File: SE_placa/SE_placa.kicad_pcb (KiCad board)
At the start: 2 copper layers, 142.2 x 71.1 mm, 58 parts, among them J1 Bateria 3.3V, J3 Conn_02x07_ESP32_IO, J4 Conn_02x03_LORA_IO, J5 UART, J6 U.FL-R-SMT(01), J7 I2C-0, J8 I2C-1, J9 Micro_SD_Card_Det_Hirose_DM3AT, Q1 BSS138, Q2 BSS138, SW1 SW_Push_Download, SW2 SW_Push_ESP_RST, U1 ESP32-WROVER, U2 RFM95W-915S2

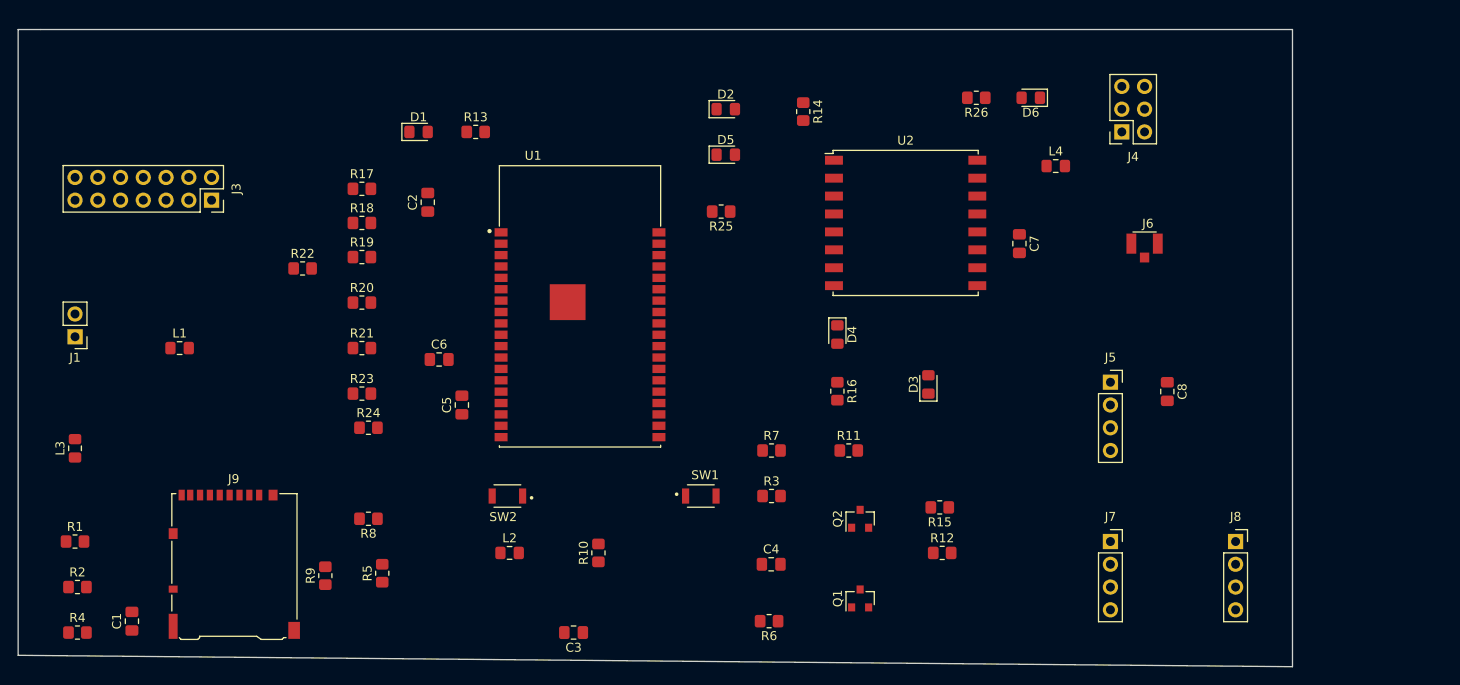
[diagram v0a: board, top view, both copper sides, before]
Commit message: Actualizacion de PCB solo rutas
Eliminado un led repetido, el led 5. Primer intento crudo de desarrollar la PCB sin estandares, tamaños de caminos u otras consideraciones tecnicas, solo ruteo para ir entendiendo y aprendiendo cual es la mejor ubicacion de los elementos, tambien saber si puedo llegar en algun momento a la meta de 52 mm X 40 mm.
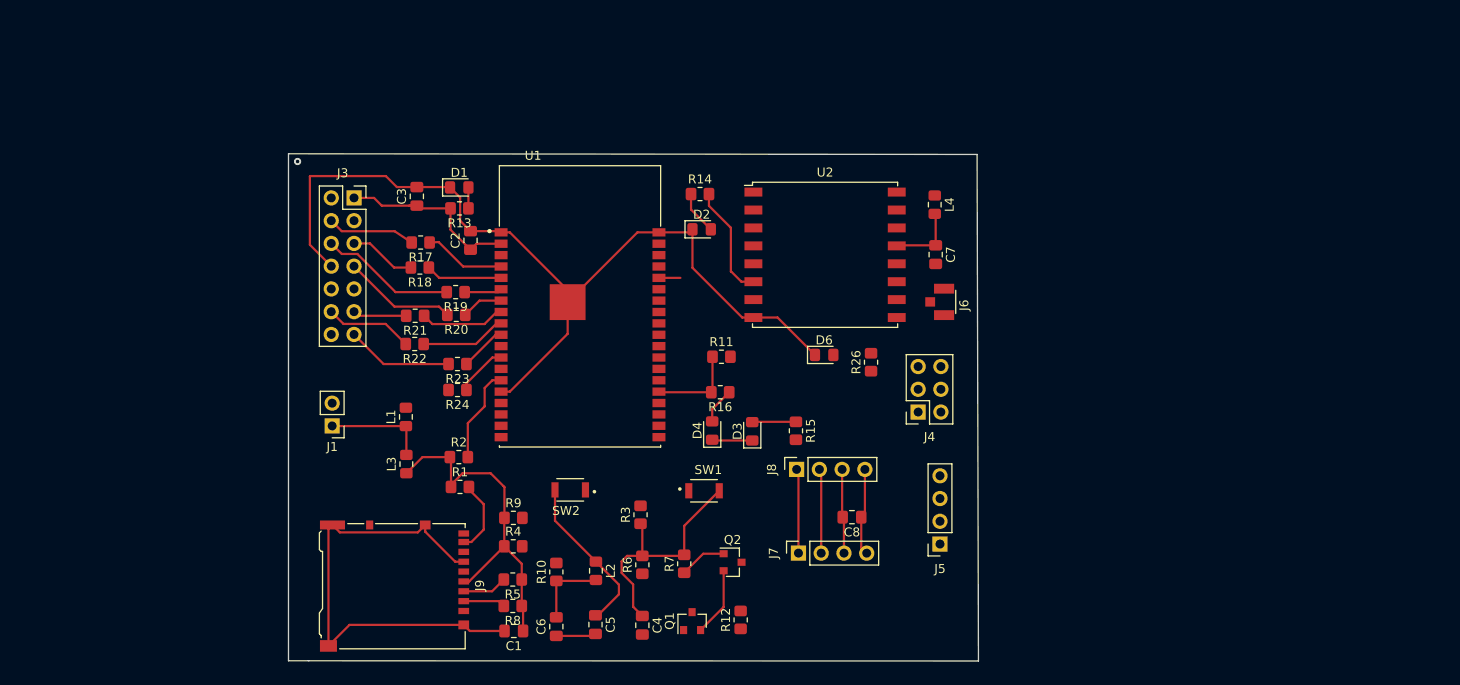
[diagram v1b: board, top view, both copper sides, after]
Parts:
- removed D5: LED, LED_SMD:LED_0805_2012Metric_Pad1.15x1.40mm_HandSolder
- removed R25: 2K, Resistor_SMD:R_0805_2012Metric_Pad1.20x1.40mm_HandSolder
- moved C3 51.7 mm to (138.5, 37.7), turned to 90 degrees
- moved J8 49.7 mm to (180.9, 68.1), turned to 90 degrees
- moved R4 49.6 mm to (149.2, 76.7)
- moved R2 45.0 mm to (143.2, 66.8)
- moved R1 43.4 mm to (143.3, 70.1)
- moved C1 42.6 mm to (149.3, 86.2), turned to 180 degrees
- moved J4 38.7 mm to (194.4, 61.7)
- moved C8 37.9 mm to (187.0, 73.5), turned to 180 degrees
- moved L3 37.0 mm to (137.3, 67.6)
- moved D6 36.8 mm to (183.9, 55.4), turned to 0 degrees
- moved J7 34.8 mm to (181.1, 77.5), turned to 90 degrees
- moved C6 32.6 mm to (154.1, 85.7), turned to 90 degrees
- moved R26 31.8 mm to (189.2, 56.2), turned to 90 degrees
- moved J1 30.4 mm to (129.0, 63.3)
- moved C5 28.7 mm to (158.4, 85.5), turned to 270 degrees
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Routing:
- net GND: track 0.00 -> 179.4 mm
- net Net-(C1-Pad1): track 0.00 -> 39.7 mm
- net /VCC-ESP: track 0.00 -> 31.3 mm
- net Net-(C4-Pad1): track 0.00 -> 26.8 mm
- net Net-(C5-Pad1): track 0.00 -> 18.2 mm
- net /IO34-I34: track 0.00 -> 15.1 mm
- net /IO35-I35: track 0.00 -> 12.7 mm
- net /SPI1-RST: track 0.00 -> 12.6 mm
- net /IO25: track 0.00 -> 11.9 mm
- net +3V3: track 0.00 -> 11.5 mm
- net /SPI2-MISO: track 0.00 -> 10.7 mm
- net /IO2: track 0.00 -> 9.89 mm
- net /IO36-I36: track 0.00 -> 9.84 mm
- net /IO33: track 0.00 -> 9.81 mm
- net Net-(R22-Pad1): track 0.00 -> 9.60 mm
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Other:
- board size 142.2 x 71.1 mm -> 77 x 56.6 mm

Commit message: reinicio de ruteo
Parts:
- moved L3 4.63 mm to (132.7, 67.1)
- moved L1 4.56 mm to (132.7, 62.3)
- moved R10 1.51 mm to (154.1, 81.1)
- moved R2 0.68 mm to (143.2, 66.1)
- moved C3 0.43 mm to (138.5, 38.1)
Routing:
- net GND: track 179.4 -> 0.00 mm
- net Net-(C1-Pad1): track 39.7 -> 0.00 mm
- net /VCC-ESP: track 31.3 -> 0.00 mm
- net Net-(C4-Pad1): track 26.8 -> 0.00 mm
- net Net-(C5-Pad1): track 18.2 -> 0.00 mm
- net /IO34-I34: track 15.1 -> 0.00 mm
- net /IO35-I35: track 12.7 -> 0.00 mm
- net /SPI1-RST: track 12.6 -> 0.00 mm
- net /IO25: track 11.9 -> 0.00 mm
- net +3V3: track 11.5 -> 0.00 mm
- net /SPI2-MISO: track 10.7 -> 0.00 mm
- net /IO2: track 9.89 -> 0.00 mm
- net /IO36-I36: track 9.84 -> 0.00 mm
- net /IO33: track 9.81 -> 0.00 mm
- net Net-(R22-Pad1): track 9.60 -> 0.00 mm
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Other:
- net class Default: clearance 0.2 -> 0.3
- net class PWR added: clearance 0.3, trace_width 0.5, via_dia 0.8, via_drill 0.4
- rule trace_clearance: 0.2 -> 0.3

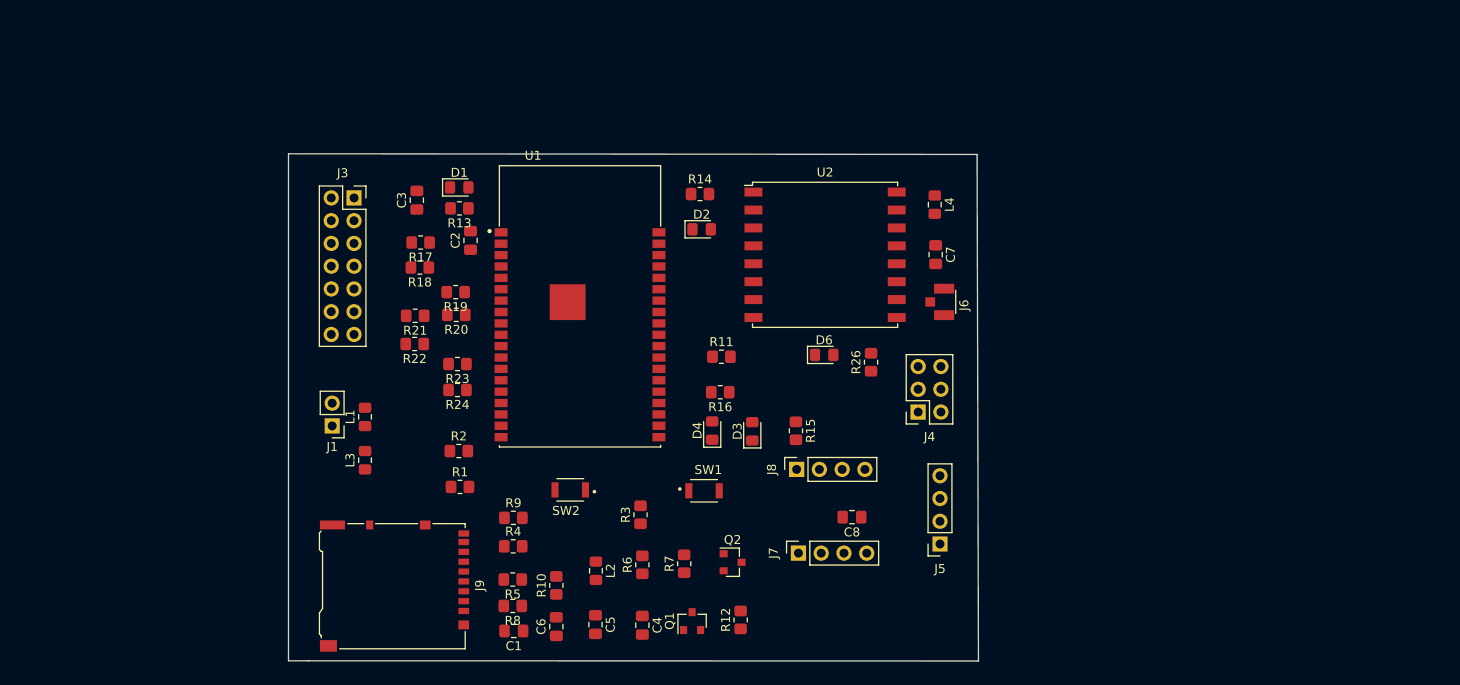
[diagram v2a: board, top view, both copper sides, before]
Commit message: Corregida Grid, reinciado el PCB
Crroegido grid a 25 mil, reconectado el layout, se cambiaron ubicación de algunos elementos dentro de la sabana . se retiraron las resistencias de 0 ohm no necesarias en la I/O, se cambio bonina por resistencia de p ohm en diagrama reset se agregó resistencias pull up a I2C, , se reitaron resistencias pull up no necesarias en la conexion de la Micro SD. Se organizaron las fuentes de todo el circuito, 3.3V Alimentación 3V3 punto de conexion ESP  y 3.3VP punto de conexion Lora.
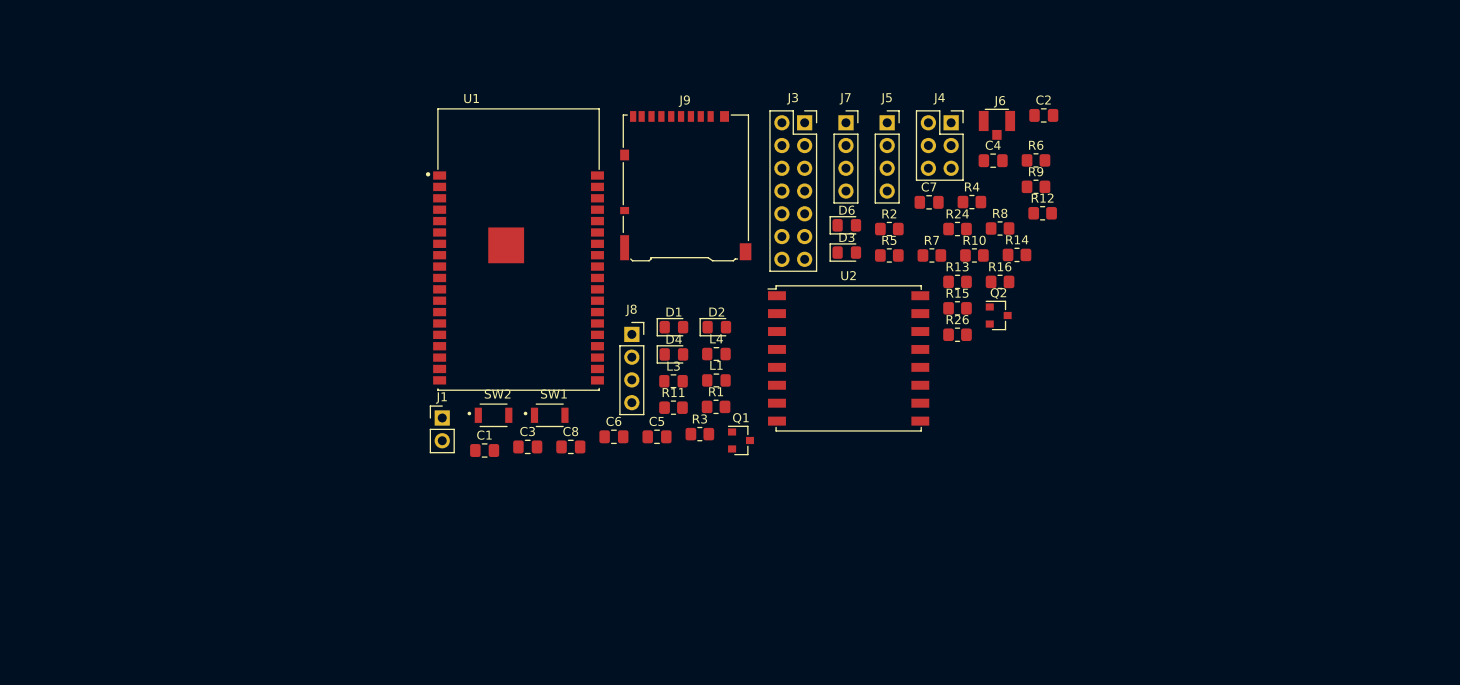
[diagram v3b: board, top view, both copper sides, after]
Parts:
- removed L2: 2A 120 ohm, Inductor_SMD:L_0805_2012Metric_Pad1.15x1.40mm_HandSolder
- removed R17, R18, R19, R20, R21, R22, R23: 0R(1%), Resistor_SMD:R_0805_2012Metric_Pad1.20x1.40mm_HandSolder
- moved R9 69.0 mm to (207.6, 36.6)
- moved R8 68.8 mm to (203.6, 41.3), turned to 0 degrees
- moved C2 65.5 mm to (208.5, 28.6), turned to 0 degrees
- moved C4 65.0 mm to (202.8, 33.7), turned to 0 degrees
- moved R4 64.0 mm to (200.4, 38.3)
- moved R6 63.0 mm to (207.6, 33.7), turned to 0 degrees
- moved R10 59.5 mm to (200.7, 44.3), turned to 0 degrees
- moved R24 58.6 mm to (198.8, 41.3), turned to 0 degrees
- moved R12 56.5 mm to (208.3, 39.6), turned to 0 degrees
- moved R13 56.2 mm to (198.8, 47.2), turned to 0 degrees
- moved R5 55.5 mm to (191.2, 44.3), turned to 0 degrees
- moved J9 55.3 mm to (168.5, 36.5), turned to 0 degrees
- moved R2 54.1 mm to (191.2, 41.3)
- moved J3 51.0 mm to (181.8, 29.5)
- moved J7 48.3 mm to (186.4, 29.5), turned to 0 degrees
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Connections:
- C2 pad 1: /VCC-ESP -> +3V3
- C3 pad 1: /VCC-ESP -> +3V3
- C7 pad 1: /VCC-LORA -> Net-(C7-Pad1)
- L1 pad 2: /VCC-ESP -> +3V3
- L4 pad 2: /VCC-LORA -> Net-(C7-Pad1)
- R24 pad 1: Net-(R24-Pad1) -> /ESP-EN
- R24 pad 2: /IO12 -> Net-(C5-Pad1)
- U1 pad 10: Net-(R23-Pad1) -> /IO25
- U1 pad 12: Net-(R24-Pad1) -> /IO12
- U1 pad 2: /VCC-ESP -> +3V3
- U1 pad 4: Net-(R17-Pad1) -> /IO36-I36
- U1 pad 5: Net-(R18-Pad1) -> /IO39-I39
- U1 pad 6: Net-(R19-Pad1) -> /IO34-I34
- U1 pad 7: Net-(R20-Pad1) -> /IO35-I35
- U1 pad 8: Net-(R21-Pad1) -> /IO32
- U1 pad 9: Net-(R22-Pad1) -> /IO33
- U2 pad 13: /VCC-LORA -> Net-(C7-Pad1)
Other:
- board outline removed

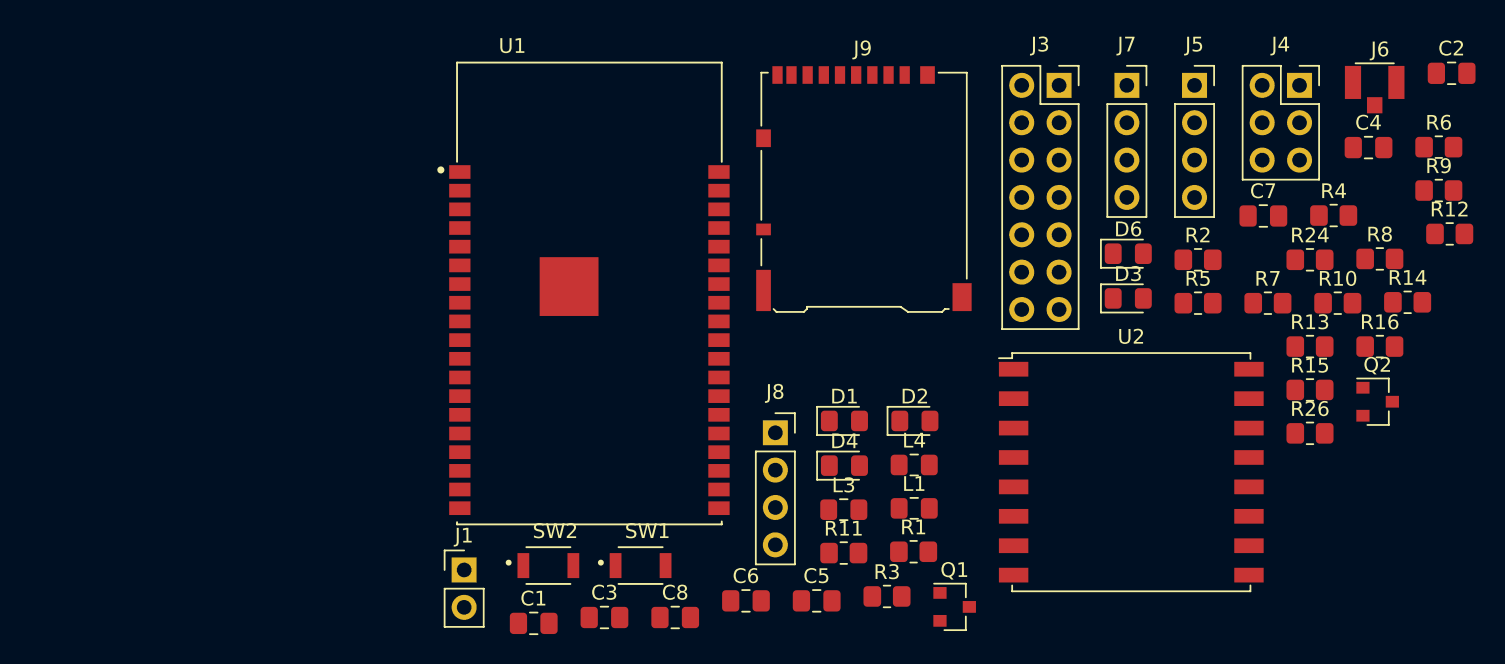
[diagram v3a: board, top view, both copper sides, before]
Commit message: Actualizacion PCB
Organizo archivos, agrego nuevos elementos a footprint, actualizo net list y actualizo PCB, agrego modelos 3D disponibles. Listo para iniciar ruteo
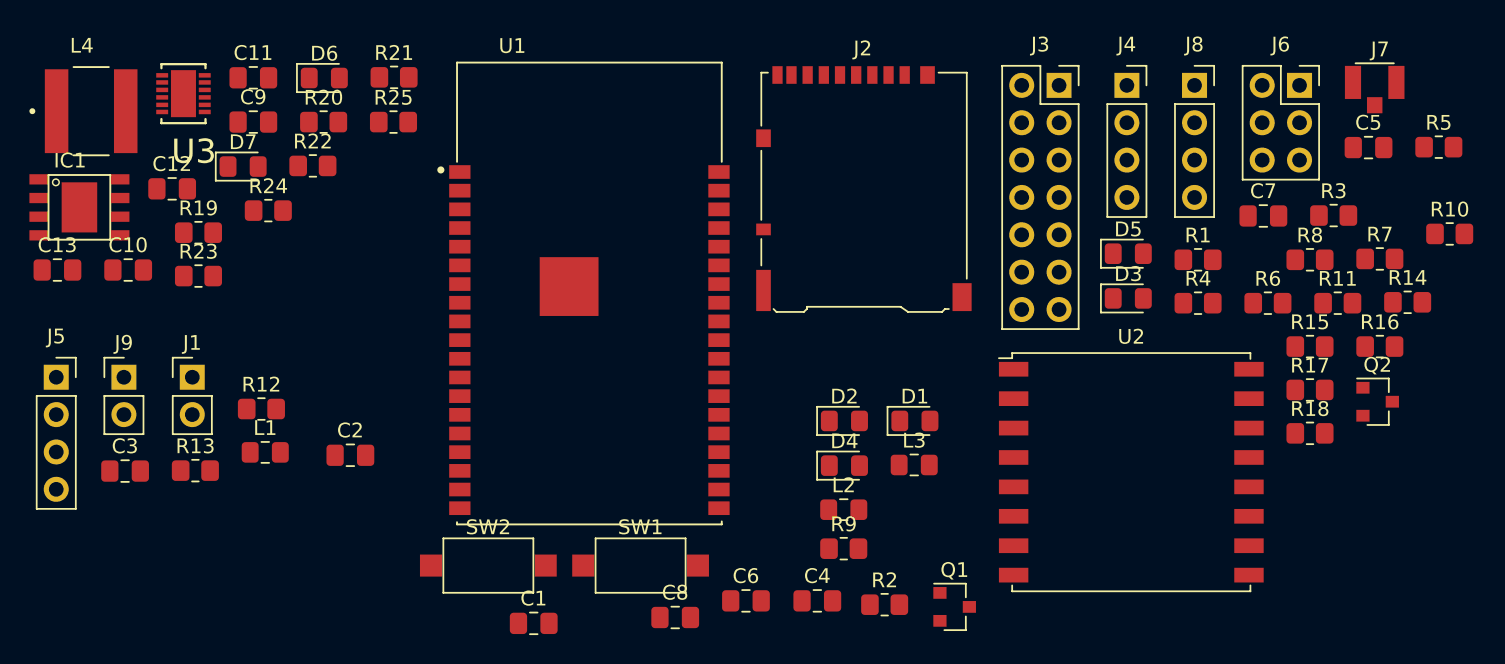
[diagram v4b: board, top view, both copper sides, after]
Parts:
- removed the J8 at (162.5, 53.1)
- removed the R1 at (171.9, 61.2)
- removed the R11 at (167.1, 61.3)
- removed the R3 at (170.1, 64.2)
- added C10: 10uF, Capacitor_SMD:C_0805_2012Metric_Pad1.18x1.45mm_HandSolder, F.Cu at (118.5, 42.0)
- added C11: 10uF, Capacitor_SMD:C_0805_2012Metric_Pad1.18x1.45mm_HandSolder, F.Cu at (127.0, 28.9)
- added C12: 1.5nF, Capacitor_SMD:C_0805_2012Metric_Pad1.18x1.45mm_HandSolder, F.Cu at (121.5, 36.5)
- added C13: 22uF, Capacitor_SMD:C_0805_2012Metric_Pad1.18x1.45mm_HandSolder, F.Cu at (113.7, 42.0)
- added C9: 10uF, Capacitor_SMD:C_0805_2012Metric_Pad1.18x1.45mm_HandSolder, F.Cu at (127.0, 32.0)
- added D6: LED, LED_SMD:LED_0805_2012Metric_Pad1.15x1.40mm_HandSolder, F.Cu at (131.8, 29.0)
- added D7: LED, LED_SMD:LED_0805_2012Metric_Pad1.15x1.40mm_HandSolder, F.Cu at (126.3, 35.0)
- added IC1: TP4056, TP4056:SOP-8, F.Cu at (115.2, 37.8)
- added J5: I2C-1, Connector_PinSocket_2.54mm:PinSocket_1x04_P2.54mm_Vertical, F.Cu at (113.6, 49.3)
- added J9: Connector Bateria, Connector_PinHeader_2.54mm:PinHeader_1x02_P2.54mm_Vertical, F.Cu at (118.2, 49.3)
- added L4: 4.7 uH, 1264EY-4R7M_P3:IND_1264EY-4R7M=P3, F.Cu at (116.0, 31.2)
- added R10: 0R(1%), Resistor_SMD:R_0805_2012Metric_Pad1.20x1.40mm_HandSolder, F.Cu at (208.3, 39.6)
- added R13: 4.7K(5%), Resistor_SMD:R_0805_2012Metric_Pad1.20x1.40mm_HandSolder, F.Cu at (123.0, 55.7)
- added R19: 0.4 ohm, Resistor_SMD:R_0805_2012Metric_Pad1.20x1.40mm_HandSolder, F.Cu at (123.3, 39.5)
- added R2: 10K(1%), Resistor_SMD:R_0805_2012Metric_Pad1.20x1.40mm_HandSolder, F.Cu at (169.9, 64.8)
- added R20: 2K, Resistor_SMD:R_0805_2012Metric_Pad1.20x1.40mm_HandSolder, F.Cu at (131.8, 32.0)
- added R21: 2K, Resistor_SMD:R_0805_2012Metric_Pad1.20x1.40mm_HandSolder, F.Cu at (136.6, 28.9)
- added R22: 8.2K, Resistor_SMD:R_0805_2012Metric_Pad1.20x1.40mm_HandSolder, F.Cu at (131.0, 34.9)
- added R23: 15K, Resistor_SMD:R_0805_2012Metric_Pad1.20x1.40mm_HandSolder, F.Cu at (123.3, 42.4)
- added R24: 340K, Resistor_SMD:R_0805_2012Metric_Pad1.20x1.40mm_HandSolder, F.Cu at (128.0, 38.0)
- added R25: 200K, Resistor_SMD:R_0805_2012Metric_Pad1.20x1.40mm_HandSolder, F.Cu at (136.5, 32.0)
- added U3: LTC3441EDEPBF, LTC3441EDEPBF:DFN400X300X80-13N, F.Cu at (122.2, 30.0)
- J1: value Bateria 3.3V -> 5V
- R12: value 0R(1%) -> 4.7K(5%)
- R9: value 10K -> 0R(1%)
- SW1, SW2: footprint B3U-1000P:SW_B3U-1000P -> Button_Switch_SMD:SW_SPST_CK_RS282G05A3
- moved R12 81.7 mm to (127.5, 51.5)
- moved C2 79.3 mm to (133.6, 54.6)
- moved R9 47.2 mm to (167.1, 61.0)
- moved L1 44.3 mm to (127.8, 54.4)
- moved C3 34.1 mm to (118.3, 55.7)
- moved J1 22.7 mm to (122.8, 49.3)
- moved SW2 4.08 mm to (143.0, 62.1)
- renumbered C5 to C4, C4 to C5, D2 to D1, D1 to D2, D6 to D5, J9 to J2, J7 to J4, J4 to J6, J6 to J7, J5 to J8, L3 to L2, L4 to L3, R2 to R1, R10 to R11, R13 to R15, R15 to R17, R26 to R18, R4 to R3, R5 to R4, R6 to R5, R7 to R6, R8 to R7, R24 to R8
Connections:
- net /IO34-I34 renamed /I34
- net /IO35-I35 renamed /I35
- net /IO36-I36 renamed /I36
- net /IO39-I39 renamed /I39
- C7 pad 1: Net-(C7-Pad1) -> +3.3VP
- C8 pad 1: /VCC-ESP -> +3V3
- J1 pad 1: +3V3 -> +5V
- J2 pad 1: Net-(J9-Pad1) -> Net-(J2-Pad1)
- J3 pad 1: /VCC-ESP -> +3V3
- J3 pad 10: GND -> Net-(J3-Pad10)
- J3 pad 2: /VCC-ESP -> +3V3
- J3 pad 3: /VCC-ESP -> +3V3
- J3 pad 8: GND -> Net-(J3-Pad10)
- J3 pad 9: GND -> Net-(J3-Pad10)
- J4 pad 4: /VCC-ESP -> +3V3
- J6 pad 1: /VCC-LORA -> +3.3VP
- J6 pad 2: /VCC-LORA -> +3.3VP
- J8 pad 1: /VCC-ESP -> +3V3
- L3 pad 2: Net-(C7-Pad1) -> +3.3VP
- R11 pad 2: /VCC-ESP -> +3V3
- R12 pad 1: /IO0 -> /I2C-SDA
- R12 pad 2: Net-(Q1-Pad3) -> +3V3
- R15 pad 2: /VCC-ESP -> +3V3
- R18 pad 2: /VCC-LORA -> +3.3VP
- R9 pad 1: Net-(C1-Pad1) -> /IO2
- R9 pad 2: Net-(J9-Pad1) -> Net-(Q2-Pad3)
- SW1 pad 1: /VCC-ESP -> +3V3
- U1 pad 3: /EN-ESP -> /ESP-EN
- U2 pad 13: Net-(C7-Pad1) -> +3.3VP
